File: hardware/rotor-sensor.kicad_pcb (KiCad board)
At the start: 2 copper layers, 35.1 x 16.6 mm, 49 parts, among them J1 Conn_01x03, J2 Conn_01x03, U1 EE-SX199, U2 MCP2021A-xxxxSN, U3 SM351LT, U4 ATtiny202-SS, U5 AP22804AW5

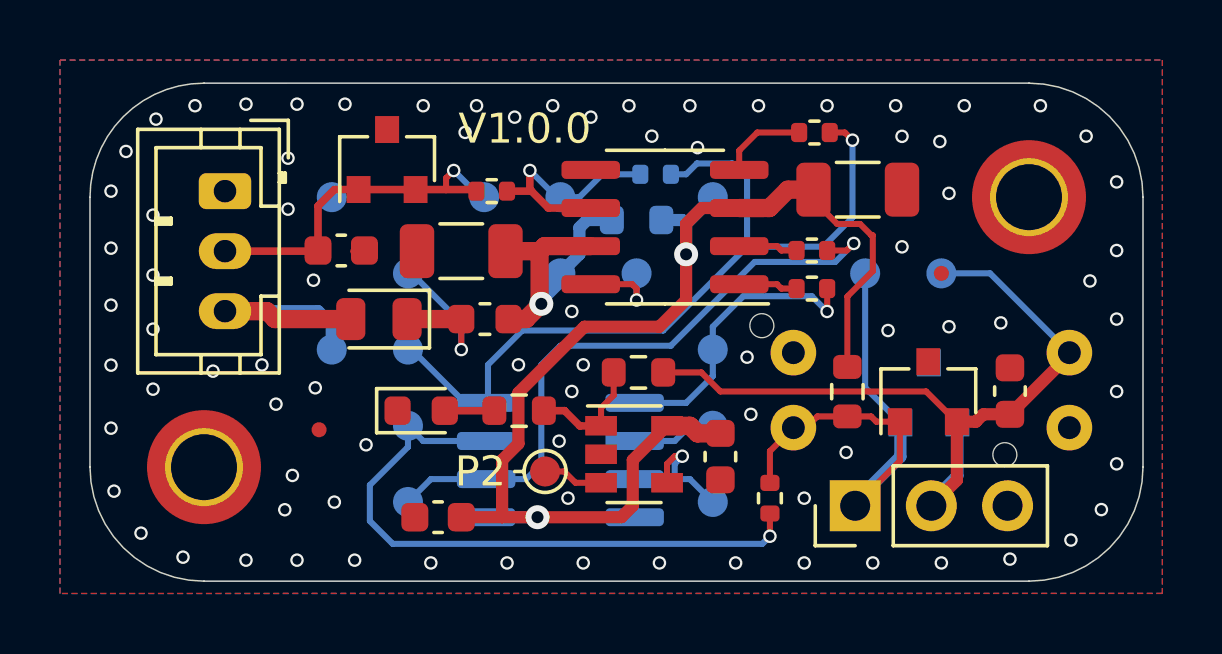
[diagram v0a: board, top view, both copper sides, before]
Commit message: KiKit downgrade
Fixes track clearance issue on panelized layout
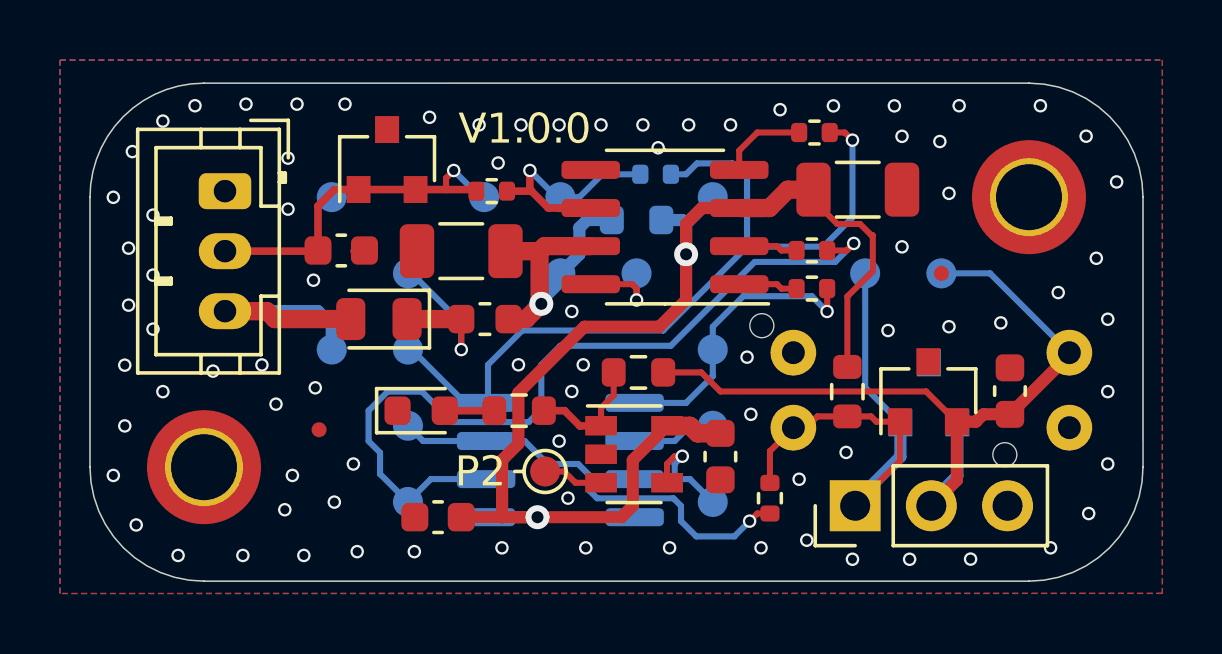
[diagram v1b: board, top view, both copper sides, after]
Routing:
- net PA7_AC0_AINP0: track 21.0 -> 14.5 mm
- net PA6_GPIO: track 21.3 -> 27.7 mm
